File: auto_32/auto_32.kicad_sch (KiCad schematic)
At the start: 6 parts, among them Q1 FDC6333C, U3 MCP2221A-I/ML, Y1 Crystal

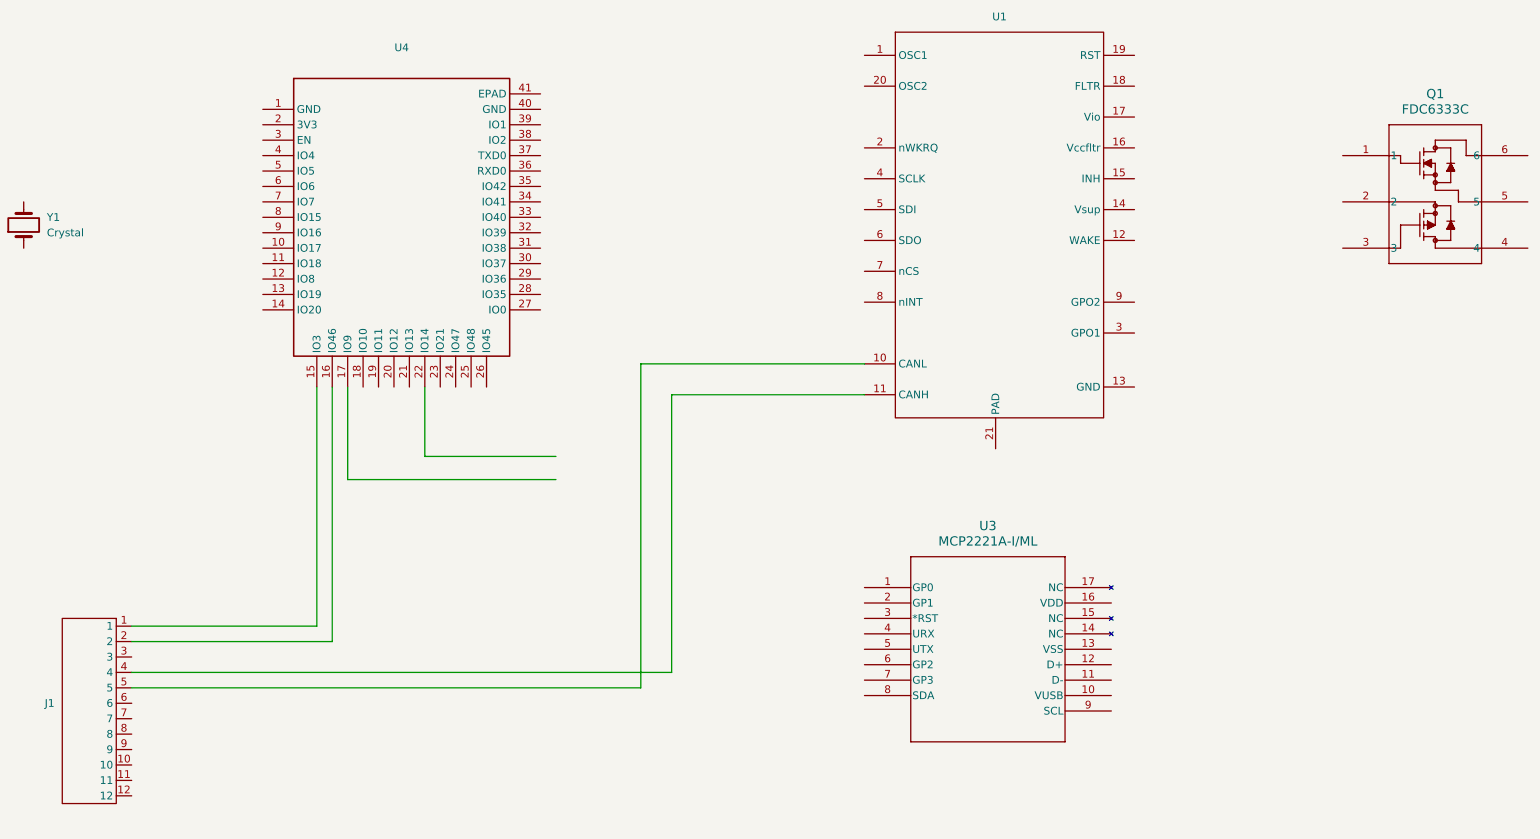
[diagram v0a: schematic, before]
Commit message: peripheral schematic added
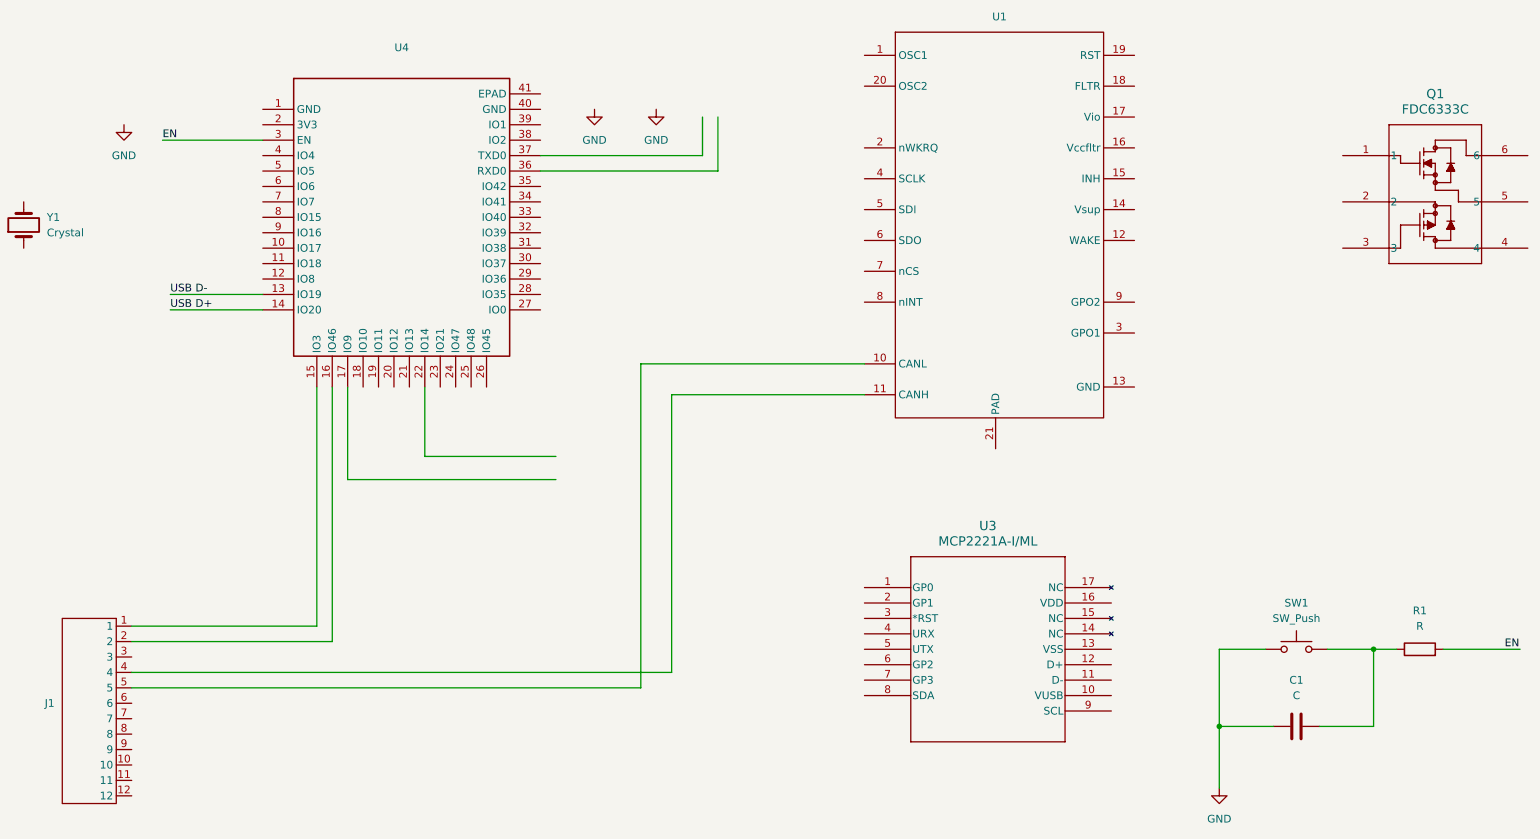
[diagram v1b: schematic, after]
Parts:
- added C1: C, symbol Device:C
- added R1: R, symbol Device:R
- added SW1: SW_Push, symbol Switch:SW_Push
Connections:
- net USB D-: now reaches U4.13 (IO19)
- net USB D+: now reaches U4.14 (IO20)
- net EN: now reaches U4.3 (EN)
- net EN: now also R1.2
- new net: C1.1, R1.1, SW1.2
- new net GND: C1.2, SW1.1

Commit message: mcu changed to rp2350
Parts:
- removed C1: C, symbol Device:C
- removed J1: ~, ssh_conn_lib:DTM13-12PA-R008, symbol ssh_conn_lib_sym:12w_conn
- removed Q1: FDC6333C, TSOT23-6_419BL_OSI, symbol ssh_Library:FDC6333C
- removed R1: R, symbol Device:R
- removed SW1: SW_Push, symbol Switch:SW_Push
- removed U1: ~, ssh_Library:VQFN-26_EP_3.5x4.5_Pitch0.5mm, symbol ssh_Library:TCAN4551RGYRQ1
- removed U3: MCP2221A-I/ML, QFN16_ML_MCH, symbol ssh_Library:MCP2221A-I_ML
- removed U4: ~, symbol ssh_Library:ESP32-S3-WROOM-1
- removed Y1: Crystal, symbol Device:Crystal
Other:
- added sheet control (control.kicad_sch)
- added sheet power (power.kicad_sch)
- added sheet power2 (untitled.kicad_sch)

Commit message: esp wroom reintroduced and can phy layer chip added
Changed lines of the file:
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@@
 	(paper "A4")
 	(sheet
-		(at -97.79 135.89)
+		(at 170.18 93.98)
 		(size 52.07 45.72)
 		(exclude_from_sim no)
@@
 		)
 		(property "Sheetname" "control"
-			(at -97.79 135.1784 0)
+			(at 170.18 93.2684 0)
 			(effects
 				(font
@@
 		)
 		(property "Sheetfile" "control.kicad_sch"
-			(at -97.79 182.1946 0)
+			(at 170.18 140.2846 0)
 			(effects
 				(font
@@
 	)
 	(sheet
-		(at -193.04 99.06)
+		(at 74.93 57.15)
 		(size 52.07 45.72)
 		(exclude_from_sim no)
@@
 		)
 		(property "Sheetname" "power2"
-			(at -193.04 98.3484 0)
+			(at 74.93 56.4384 0)
 			(effects
 				(font
@@
 		)
 		(property "Sheetfile" "untitled.kicad_sch"
-			(at -193.04 145.3646 0)
+			(at 74.93 103.4546 0)
 			(effects
 				(font
@@
 	)
 	(sheet
-		(at -97.79 66.04)
+		(at 170.18 24.13)
 		(size 52.07 45.72)
 		(exclude_from_sim no)
@@
 		)
 		(property "Sheetname" "power"
-			(at -97.79 65.3284 0)
+			(at 170.18 23.4184 0)
 			(effects
 				(font
@@
 		)
 		(property "Sheetfile" "power.kicad_sch"
-			(at -97.79 112.3446 0)
+			(at 170.18 70.4346 0)
 			(effects
 				(font
